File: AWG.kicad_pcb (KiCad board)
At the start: 2 copper layers, 140 x 75 mm, 83 parts, among them J1001 Conn_01x03, J1002 Conn_01x05, J1003 Conn_01x06, J1005 Conn_01x01, J1006 Conn_01x01, J1007 Conn_01x01, J1008 Conn_01x01, J1009 Conn_01x01, J1010 Conn_01x01, J1011 Conn_01x01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

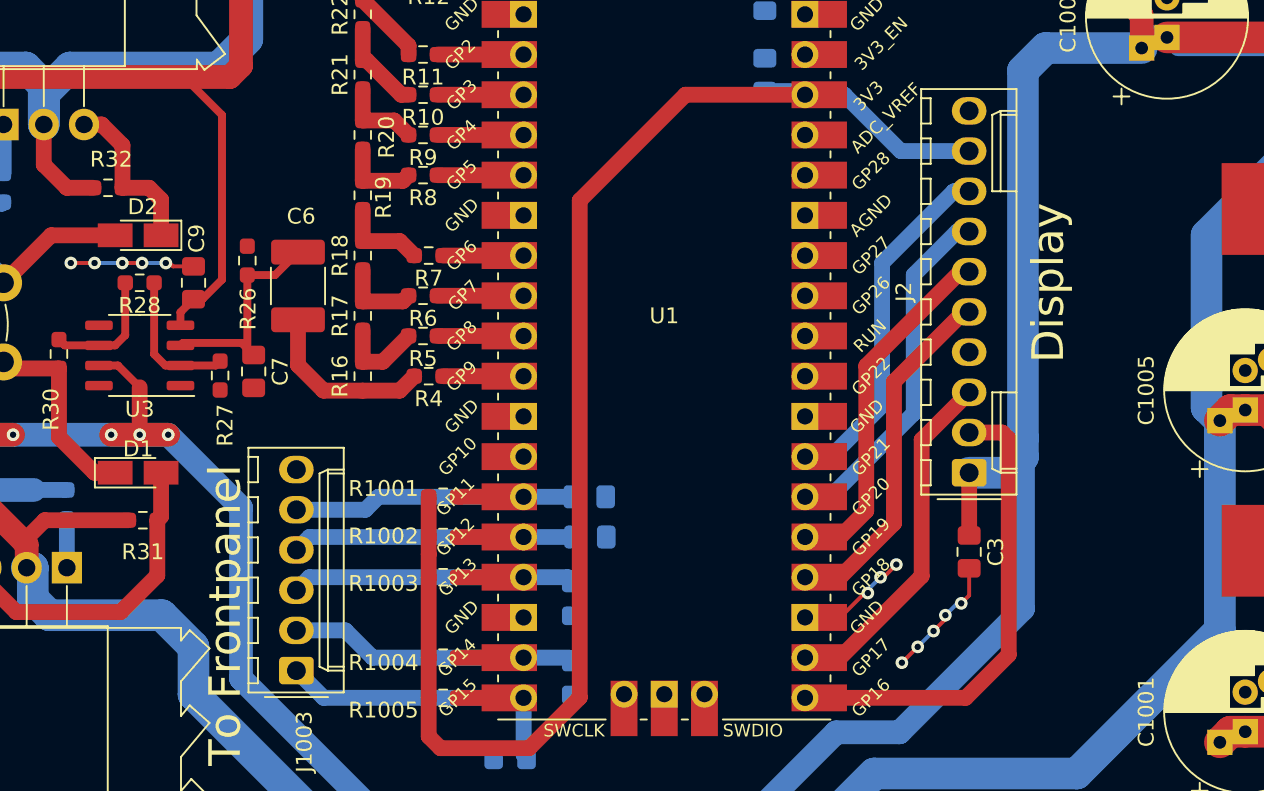
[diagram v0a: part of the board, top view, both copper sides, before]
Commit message: shorter track for R28
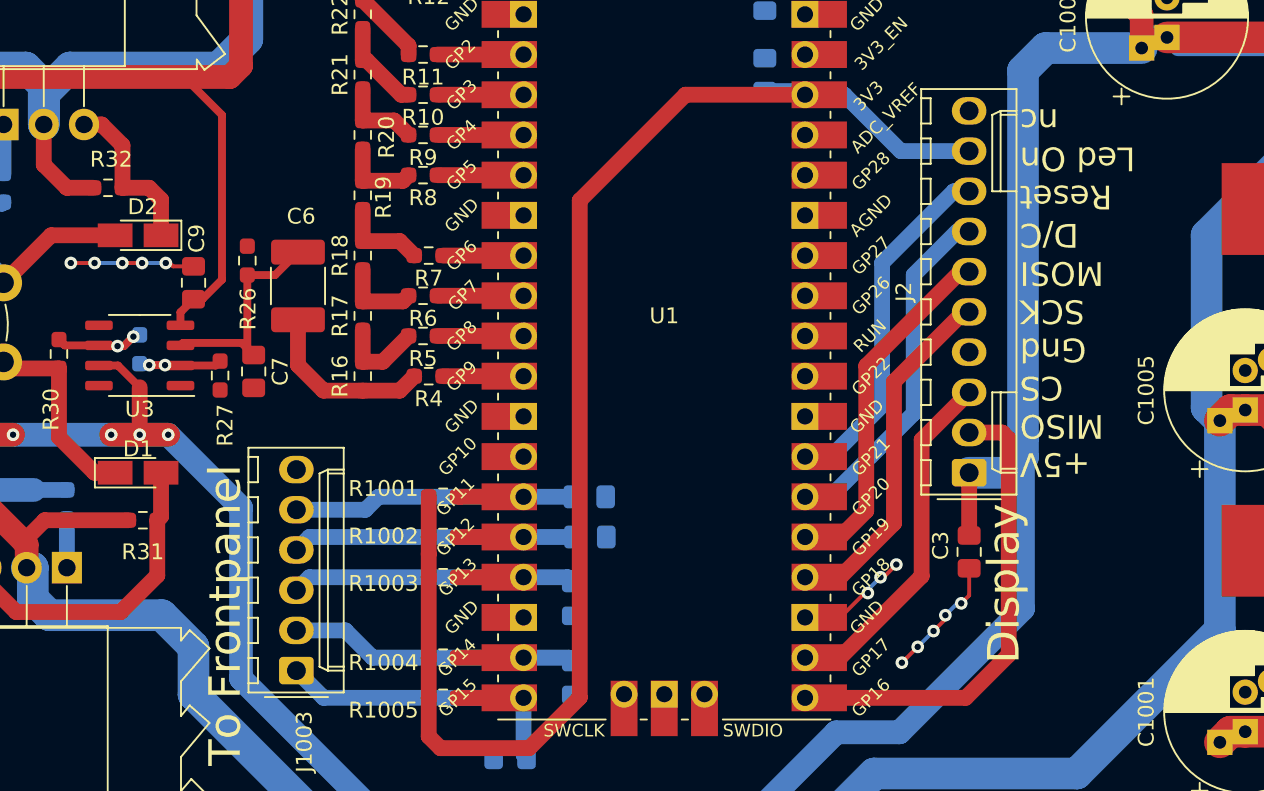
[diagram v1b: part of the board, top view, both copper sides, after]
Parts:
- R28: moved to B.Cu
- moved R28 4.20 mm to (172.6, 87.2), turned to 90 degrees
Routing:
- net Net-(R27-Pad1): track 9.09 -> 6.24 mm, vias 0 -> 2
- net Net-(R28-Pad2): track 7.92 -> 6.81 mm, vias 0 -> 2
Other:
- board text added: "+5V MISO CS Gnd SCK MOSI D/C Reset Led On nc"

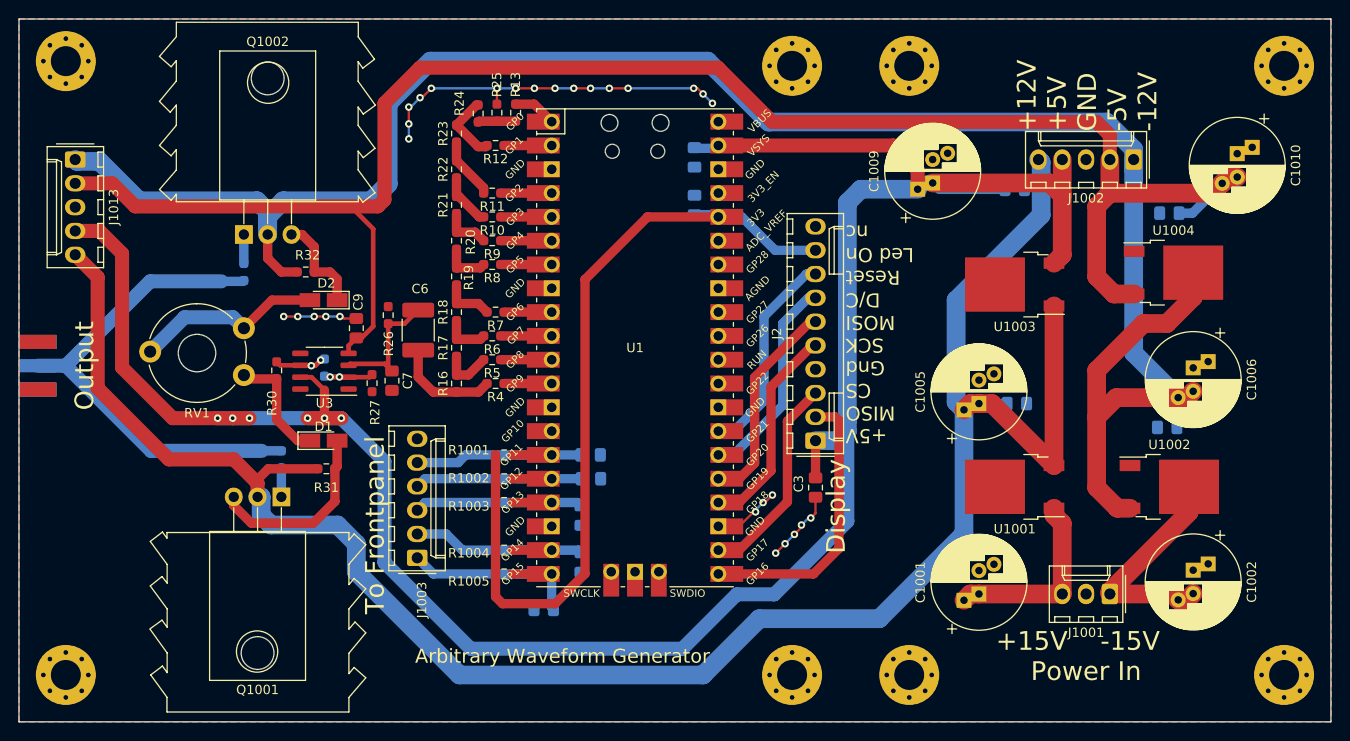
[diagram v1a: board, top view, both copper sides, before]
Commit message: R33-R34 format changed to 1210
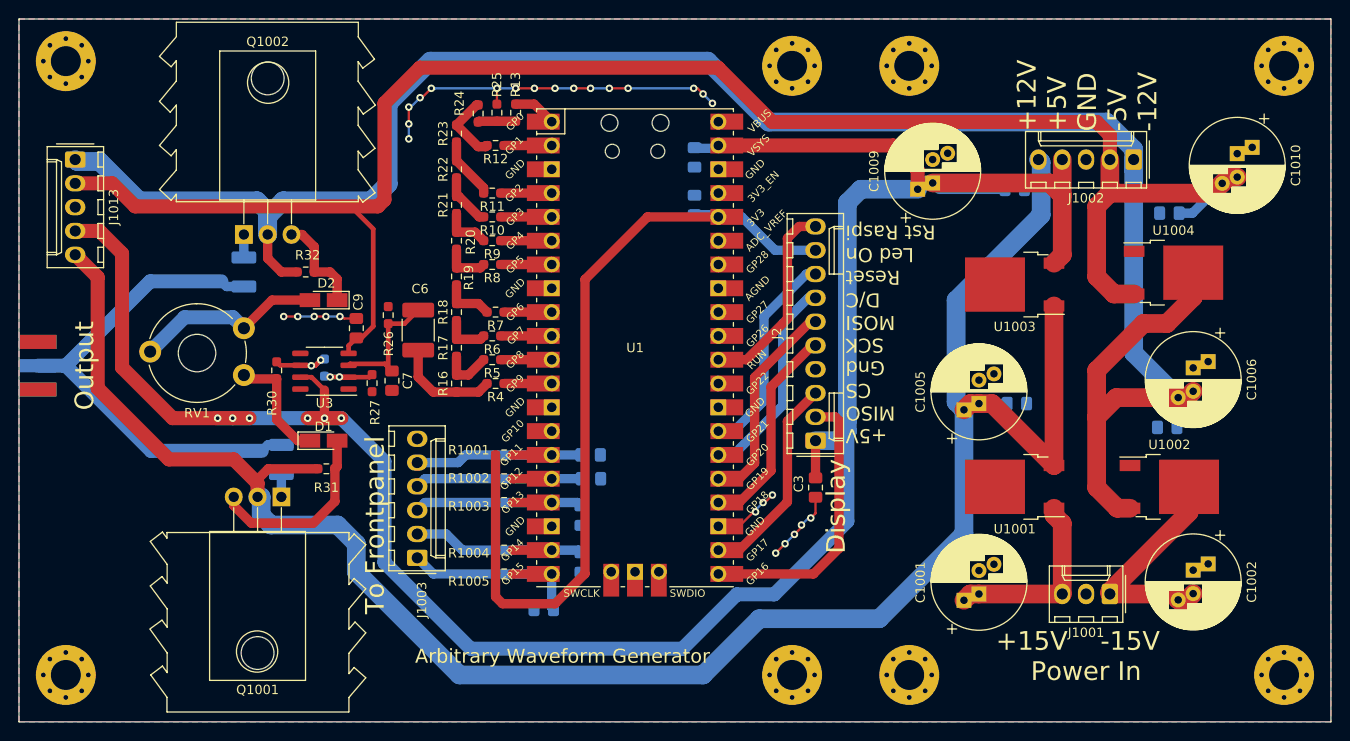
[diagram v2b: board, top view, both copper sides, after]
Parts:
- removed REF**: OSHW-Logo2_7.3x6mm_SilkScreen, Symbol:OSHW-Logo2_7.3x6mm_SilkScreen
- removed REF**: KiCad-Logo2_5mm_SilkScreen, Symbol:KiCad-Logo2_5mm_SilkScreen
- R33, R34: footprint Resistor_SMD:R_0603_1608Metric_Pad0.98x0.95mm_HandSolder -> Resistor_SMD:R_1210_3225Metric_Pad1.30x2.65mm_HandSolder
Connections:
- U1 pad 14: Net-(U1-Pad14) -> unconnected-(U1-Pad14)
- U1 pad 29: Net-(U1-Pad29) -> unconnected-(U1-Pad29)
- U1 pad 30: Net-(SW1-Pad2) -> Net-(J2-Pad10)
- U1 pad 31: Net-(U1-Pad31) -> unconnected-(U1-Pad31)
- U1 pad 32: Net-(U1-Pad32) -> unconnected-(U1-Pad32)
- U1 pad 33: Net-(U1-Pad33) -> unconnected-(U1-Pad33)
- U1 pad 34: Net-(U1-Pad34) -> unconnected-(U1-Pad34)
- U1 pad 35: Net-(U1-Pad35) -> unconnected-(U1-Pad35)
- U1 pad 37: Net-(U1-Pad37) -> unconnected-(U1-Pad37)
- U1 pad 40: Net-(U1-Pad40) -> unconnected-(U1-Pad40)
- U1 pad 41: Net-(U1-Pad41) -> unconnected-(U1-Pad41)
- U1 pad 43: Net-(U1-Pad43) -> unconnected-(U1-Pad43)
- U3 pad 1: Net-(U3-Pad1) -> unconnected-(U3-Pad1)
- U3 pad 5: Net-(U3-Pad5) -> unconnected-(U3-Pad5)
- U3 pad 8: Net-(U3-Pad8) -> unconnected-(U3-Pad8)
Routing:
- net Net-(J2-Pad10): track 0.00 -> 21.3 mm
- net Net-(Q1002-Pad1): track 3.09 -> 2.45 mm
- net Net-(Q1001-Pad1): track 3.09 -> 2.45 mm
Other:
- net class Default removed
- board text added: "+5V MISO CS Gnd SCK MOSI D/C Reset Led On Rst Raspi"
- board text removed: "+5V MISO CS Gnd SCK MOSI D/C Reset Led On nc"
